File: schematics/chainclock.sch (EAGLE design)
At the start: 17 parts, among them SW1 ROTARTY_ENCODER

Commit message: Update layout
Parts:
- removed R11, R12, R5, R6: 10k, SparkFun-Resistors:RESISTOR2010
- added R1, R2, R7, R8: 10k, SparkFun-Resistors:RESISTOREZ
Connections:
- net 3V32: now also R1.2, R2.2; no longer R11.2, R12.2
- net N$2: now also R1.1, R7.2; no longer R11.1, R5.1
- net N$5: now also R2.1, R8.2; no longer R12.1, R6.2
- net RENCA: now also ARDUNOFIO.A1, R8.1; no longer ARDUNOFIO.D12, R6.1
- net RENCB: now also ARDUNOFIO.A2, R7.1; no longer ARDUNOFIO.D11, R5.2
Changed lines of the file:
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@@
 <part name="GND10" library="SparkFun-Aesthetics" deviceset="GND" device=""/>
 <part name="GND11" library="SparkFun-Aesthetics" deviceset="GND" device=""/>
-<part name="R11" library="SparkFun-Resistors" deviceset="RESISTOR" device="2010" value="10k"/>
-<part name="R12" library="SparkFun-Resistors" deviceset="RESISTOR" device="2010" value="10k"/>
 <part name="GND12" library="SparkFun-Aesthetics" deviceset="GND" device=""/>
-<part name="R5" library="SparkFun-Resistors" deviceset="RESISTOR" device="2010" value="10k"/>
-<part name="R6" library="SparkFun-Resistors" deviceset="RESISTOR" device="2010" value="10k"/>
 <part name="GND1" library="SparkFun-Aesthetics" deviceset="GND" device=""/>
 <part name="U$4" library="desjardins" deviceset="SG30XX" device="JC"/>
+<part name="R1" library="SparkFun-Resistors" deviceset="RESISTOR" device="EZ" value="10k"/>
+<part name="R2" library="SparkFun-Resistors" deviceset="RESISTOR" device="EZ" value="10k"/>
+<part name="R7" library="SparkFun-Resistors" deviceset="RESISTOR" device="EZ" value="10k"/>
+<part name="R8" library="SparkFun-Resistors" deviceset="RESISTOR" device="EZ" value="10k"/>
 </parts>
 <sheets>
@@
 <instance part="GND10" gate="1" x="91.44" y="81.28" rot="MR0"/>
 <instance part="GND11" gate="1" x="50.8" y="81.28" rot="MR0"/>
-<instance part="R11" gate="G$1" x="76.2" y="106.68" rot="MR90"/>
-<instance part="R12" gate="G$1" x="66.04" y="106.68" rot="MR90"/>
 <instance part="GND12" gate="1" x="66.04" y="68.58"/>
-<instance part="R5" gate="G$1" x="83.82" y="96.52" rot="MR180"/>
-<instance part="R6" gate="G$1" x="58.42" y="96.52" rot="MR180"/>
 <instance part="GND1" gate="1" x="88.9" y="149.86" rot="R270"/>
 <instance part="U$4" gate="G$1" x="106.68" y="154.94"/>
+<instance part="R1" gate="G$1" x="76.2" y="106.68" rot="R90"/>
+<instance part="R2" gate="G$1" x="66.04" y="106.68" rot="R90"/>
+<instance part="R7" gate="G$1" x="83.82" y="96.52" rot="R180"/>
+<instance part="R8" gate="G$1" x="58.42" y="96.52"/>
 </instances>
 <busses>
@@
 <junction x="71.12" y="114.3"/>
 <label x="48.26" y="127" size="1.778" layer="95"/>
-<pinref part="R11" gate="G$1" pin="2"/>
-<pinref part="R12" gate="G$1" pin="2"/>
+<pinref part="R2" gate="G$1" pin="2"/>
+<pinref part="R1" gate="G$1" pin="2"/>
+<label x="68.58" y="116.84" size="1.778" layer="95"/>
 </segment>
 <segment>
@@
 <pinref part="SW1" gate="G$1" pin="B"/>
 <wire x1="76.2" y1="93.98" x2="76.2" y2="96.52" width="0.1524" layer="91"/>
+<pinref part="R1" gate="G$1" pin="1"/>
+<pinref part="R7" gate="G$1" pin="2"/>
+<wire x1="76.2" y1="96.52" x2="76.2" y2="101.6" width="0.1524" layer="91"/>
 <wire x1="76.2" y1="96.52" x2="78.74" y2="96.52" width="0.1524" layer="91"/>
-<wire x1="76.2" y1="96.52" x2="76.2" y2="101.6" width="0.1524" layer="91"/>
 <junction x="76.2" y="96.52"/>
-<pinref part="R11" gate="G$1" pin="1"/>
-<pinref part="R5" gate="G$1" pin="1"/>
 </segment>
 </net>
@@
 <wire x1="66.04" y1="96.52" x2="66.04" y2="101.6" width="0.1524" layer="91"/>
 <junction x="66.04" y="96.52"/>
-<pinref part="R12" gate="G$1" pin="1"/>
-<pinref part="R6" gate="G$1" pin="2"/>
+<pinref part="R8" gate="G$1" pin="2"/>
+<pinref part="R2" gate="G$1" pin="1"/>
 </segment>
 </net>
 <net name="RENBTN" class="0">
+<segment>
+<pinref part="SW1" gate="G$1" pin="SW+"/>
+<wire x1="76.2" y1="73.66" x2="76.2" y2="71.12" width="0.1524" layer="91"/>
+<label x="73.66" y="68.58" size="1.778" layer="95"/>
+</segment>
 <segment>
 <pinref part="ARDUNOFIO" gate="G$1" pin="D6"/>
@@
 <label x="43.18" y="182.88" size="1.778" layer="95"/>
 </segment>
-<segment>
-<pinref part="SW1" gate="G$1" pin="SW+"/>
-<wire x1="76.2" y1="73.66" x2="76.2" y2="71.12" width="0.1524" layer="91"/>
-<label x="73.66" y="68.58" size="1.778" layer="95"/>
-</segment>
 </net>
 <net name="RENCB" class="0">
 <segment>
-<pinref part="ARDUNOFIO" gate="G$1" pin="D11"/>
-<wire x1="43.18" y1="195.58" x2="45.72" y2="195.58" width="0.1524" layer="91"/>
-<label x="43.18" y="195.58" size="1.778" layer="95"/>
-</segment>
-<segment>
-<wire x1="88.9" y1="96.52" x2="91.44" y2="96.52" width="0.1524" layer="91"/>
 <wire x1="91.44" y1="96.52" x2="93.98" y2="96.52" width="0.1524" layer="91"/>
 <wire x1="91.44" y1="96.52" x2="91.44" y2="93.98" width="0.1524" layer="91"/>
-<junction x="91.44" y="96.52"/>
 <pinref part="C6" gate="G$1" pin="1"/>
 <label x="101.6" y="96.52" size="1.778" layer="95" rot="MR0"/>
-<pinref part="R5" gate="G$1" pin="2"/>
+<pinref part="R7" gate="G$1" pin="1"/>
+<wire x1="91.44" y1="96.52" x2="88.9" y2="96.52" width="0.1524" layer="91"/>
+<junction x="91.44" y="96.52"/>
+</segment>
+<segment>
+<pinref part="ARDUNOFIO" gate="G$1" pin="A2"/>
+<wire x1="12.7" y1="187.96" x2="10.16" y2="187.96" width="0.1524" layer="91"/>
+<label x="5.08" y="187.96" size="1.778" layer="95"/>
 </segment>
 </net>
 <net name="RENCA" class="0">
-<segment>
-<pinref part="ARDUNOFIO" gate="G$1" pin="D12"/>
-<wire x1="43.18" y1="198.12" x2="45.72" y2="198.12" width="0.1524" layer="91"/>
-<label x="43.18" y="198.12" size="1.778" layer="95"/>
-</segment>
 <segment>
 <wire x1="53.34" y1="96.52" x2="50.8" y2="96.52" width="0.1524" layer="91"/>
@@
 <pinref part="C5" gate="G$1" pin="1"/>
 <label x="48.26" y="96.52" size="1.778" layer="95" rot="MR0"/>
-<pinref part="R6" gate="G$1" pin="1"/>
-</segment>
-</net>
+<pinref part="R8" gate="G$1" pin="1"/>
+</segment>
+<segment>
+<pinref part="ARDUNOFIO" gate="G$1" pin="A1"/>
+<wire x1="12.7" y1="185.42" x2="10.16" y2="185.42" width="0.1524" layer="91"/>
+<label x="5.08" y="185.42" size="1.778" layer="95"/>
+</segment>
+</net>

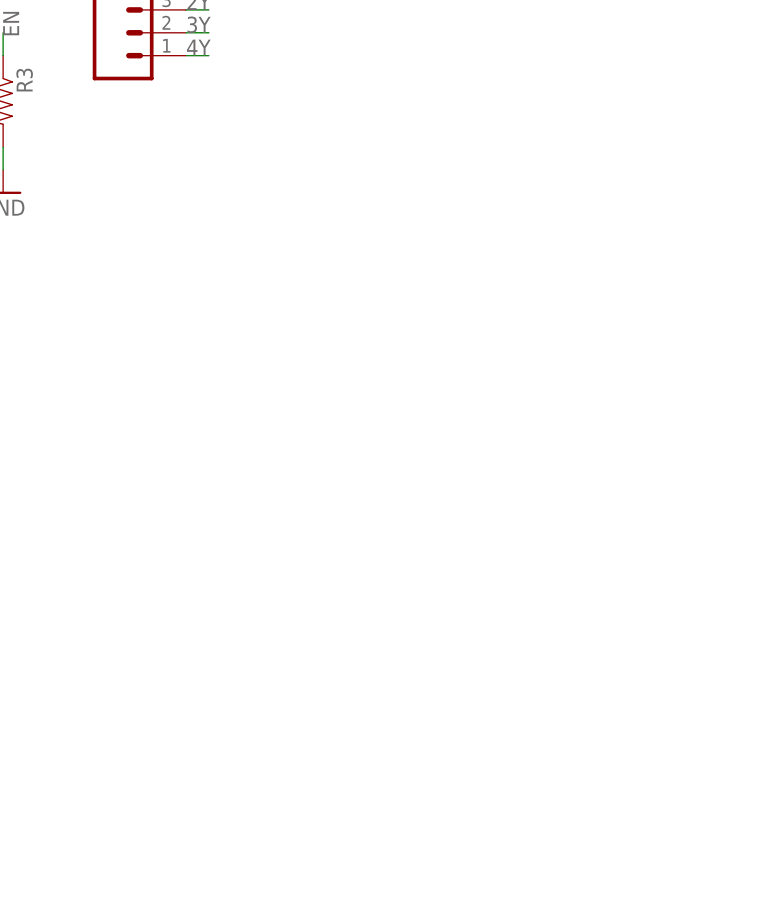
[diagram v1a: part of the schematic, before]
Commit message: Add voltage limiter for solar
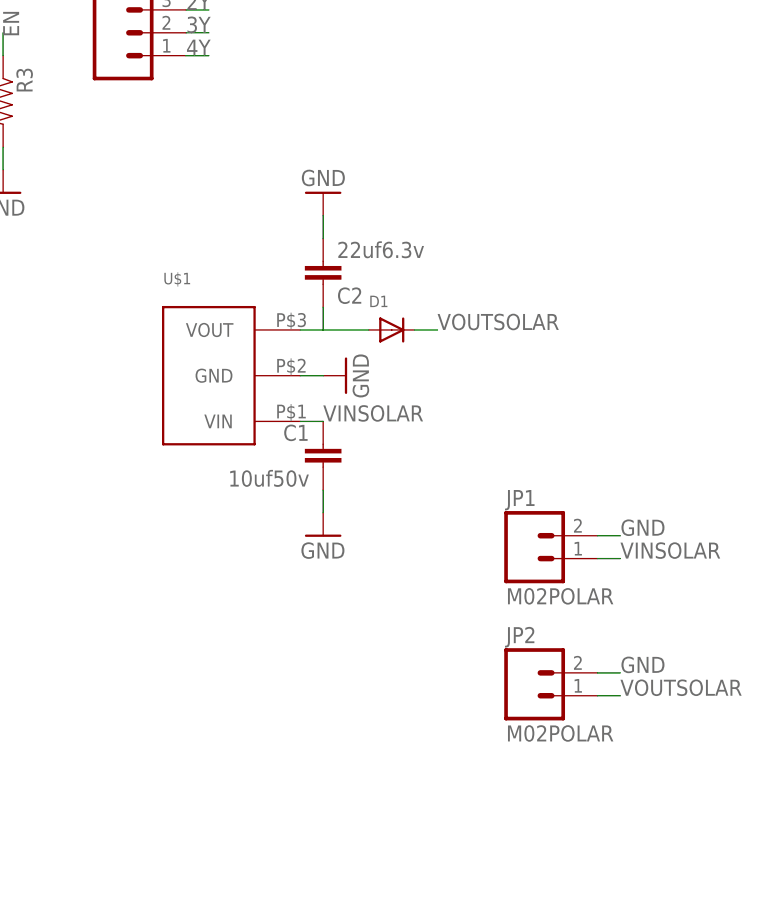
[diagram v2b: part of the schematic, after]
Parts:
- added C1: 10uf50v, SparkFun-Capacitors:CAPKIT
- added C2: 22uf6.3v, SparkFun-Capacitors:CAPKIT
- added D1: (no value), adafruit:DIODEDO-1N4148
- added JP1, JP2: M02POLAR, desjardins:M02POLAR
- added U$1: V78-500, desjardins:V78-500
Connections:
- new net N$4: C2.1, D1.A, U$1.VOUT
- new net VINSOLAR: C1.1, JP1.1, U$1.VIN
- new net VOUTSOLAR: D1.C, JP2.1
- net GND: now also C1.2, C2.2, JP1.2, JP2.2, U$1.GND
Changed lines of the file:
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@@
 <part name="R7" library="SparkFun-Resistors" deviceset="RESISTOR" device="EZ" value="10k"/>
 <part name="R8" library="SparkFun-Resistors" deviceset="RESISTOR" device="EZ" value="10k"/>
+<part name="U$1" library="desjardins" deviceset="V78-500" device=""/>
+<part name="C1" library="SparkFun-Capacitors" deviceset="CAP" device="KIT" value="10uf50v"/>
+<part name="C2" library="SparkFun-Capacitors" deviceset="CAP" device="KIT" value="22uf6.3v"/>
+<part name="GND9" library="SparkFun-Aesthetics" deviceset="GND" device=""/>
+<part name="GND13" library="SparkFun-Aesthetics" deviceset="GND" device=""/>
+<part name="GND14" library="SparkFun-Aesthetics" deviceset="GND" device=""/>
+<part name="D1" library="adafruit" deviceset="DIODE" device="DO-1N4148"/>
+<part name="JP1" library="desjardins" deviceset="M02" device="POLAR"/>
+<part name="JP2" library="desjardins" deviceset="M02" device="POLAR"/>
 </parts>
 <sheets>
@@
 <instance part="R7" gate="G$1" x="83.82" y="96.52" rot="R180"/>
 <instance part="R8" gate="G$1" x="58.42" y="96.52"/>
+<instance part="U$1" gate="G$1" x="213.36" y="154.94"/>
+<instance part="C1" gate="G$1" x="226.06" y="144.78" rot="MR0"/>
+<instance part="C2" gate="G$1" x="226.06" y="167.64" rot="MR180"/>
+<instance part="GND9" gate="1" x="226.06" y="137.16"/>
+<instance part="GND13" gate="1" x="226.06" y="175.26" rot="R180"/>
+<instance part="GND14" gate="1" x="228.6" y="154.94" rot="R90"/>
+<instance part="D1" gate="G$1" x="233.68" y="160.02"/>
+<instance part="JP1" gate="G$1" x="248.92" y="134.62"/>
+<instance part="JP2" gate="G$1" x="248.92" y="119.38"/>
 </instances>
 <busses>
@@
 <pinref part="GND1" gate="1" pin="GND"/>
 <pinref part="U$4" gate="G$1" pin="GND"/>
+</segment>
+<segment>
+<pinref part="U$1" gate="G$1" pin="GND"/>
+<wire x1="223.52" y1="154.94" x2="226.06" y2="154.94" width="0.1524" layer="91"/>
+<pinref part="GND14" gate="1" pin="GND"/>
+</segment>
+<segment>
+<wire x1="256.54" y1="137.16" x2="259.08" y2="137.16" width="0.1524" layer="91"/>
+<label x="259.08" y="137.16" size="1.778" layer="95"/>
+<pinref part="JP1" gate="G$1" pin="2"/>
+</segment>
+<segment>
+<wire x1="256.54" y1="121.92" x2="259.08" y2="121.92" width="0.1524" layer="91"/>
+<label x="259.08" y="121.92" size="1.778" layer="95"/>
+<pinref part="JP2" gate="G$1" pin="2"/>
+</segment>
+<segment>
+<pinref part="C1" gate="G$1" pin="2"/>
+<wire x1="226.06" y1="142.24" x2="226.06" y2="139.7" width="0.1524" layer="91"/>
+<pinref part="GND9" gate="1" pin="GND"/>
+</segment>
+<segment>
+<pinref part="C2" gate="G$1" pin="2"/>
+<wire x1="226.06" y1="170.18" x2="226.06" y2="172.72" width="0.1524" layer="91"/>
+<pinref part="GND13" gate="1" pin="GND"/>
 </segment>
 </net>
@@
 </segment>
 </net>
+<net name="VOUTSOLAR" class="0">
+<segment>
+<wire x1="256.54" y1="119.38" x2="259.08" y2="119.38" width="0.1524" layer="91"/>
+<label x="259.08" y="119.38" size="1.778" layer="95"/>
+<pinref part="JP2" gate="G$1" pin="1"/>
+</segment>
+<segment>
+<pinref part="D1" gate="G$1" pin="C"/>
+<wire x1="236.22" y1="160.02" x2="238.76" y2="160.02" width="0.1524" layer="91"/>
+<label x="238.76" y="160.02" size="1.778" layer="95"/>
+</segment>
+</net>
+<net name="VINSOLAR" class="0">
+<segment>
+<pinref part="U$1" gate="G$1" pin="VIN"/>
+<wire x1="223.52" y1="149.86" x2="226.06" y2="149.86" width="0.1524" layer="91"/>
+<label x="226.06" y="149.86" size="1.778" layer="95"/>
+<pinref part="C1" gate="G$1" pin="1"/>
+</segment>
+<segment>
+<wire x1="256.54" y1="134.62" x2="259.08" y2="134.62" width="0.1524" layer="91"/>
+<label x="259.08" y="134.62" size="1.778" layer="95"/>
+<pinref part="JP1" gate="G$1" pin="1"/>
+</segment>
+</net>
+<net name="N$4" class="0">
+<segment>
+<pinref part="U$1" gate="G$1" pin="VOUT"/>
+<pinref part="D1" gate="G$1" pin="A"/>
+<wire x1="223.52" y1="160.02" x2="226.06" y2="160.02" width="0.1524" layer="91"/>
+<pinref part="C2" gate="G$1" pin="1"/>
+<wire x1="226.06" y1="160.02" x2="231.14" y2="160.02" width="0.1524" layer="91"/>
+<wire x1="226.06" y1="160.02" x2="226.06" y2="162.56" width="0.1524" layer="91"/>
+</segment>
+</net>

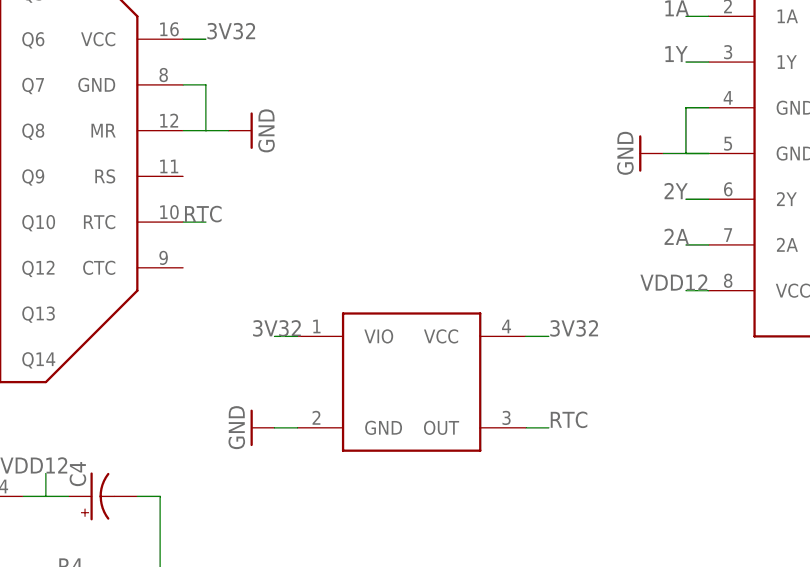
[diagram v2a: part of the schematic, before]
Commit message: Updates to the counter
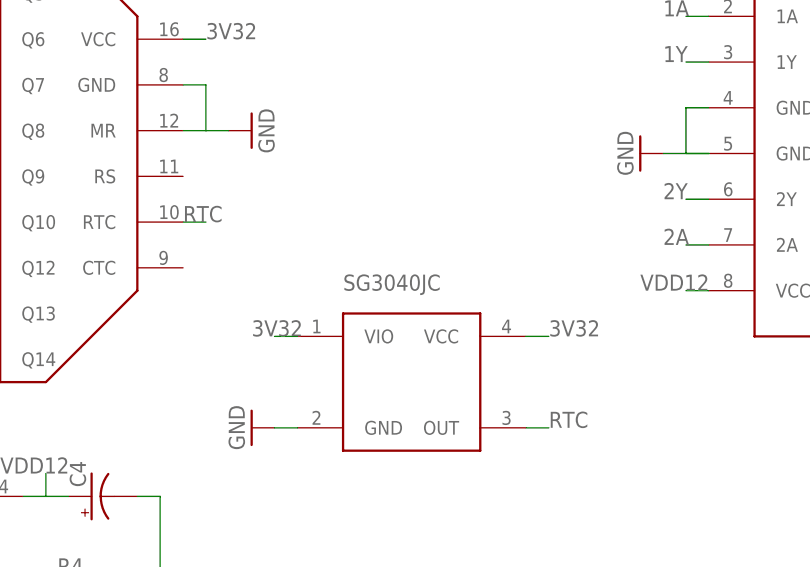
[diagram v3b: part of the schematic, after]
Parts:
- renumbered U$4 to SG3040JC
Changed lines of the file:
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@@
 <part name="GND12" library="SparkFun-Aesthetics" deviceset="GND" device=""/>
 <part name="GND1" library="SparkFun-Aesthetics" deviceset="GND" device=""/>
-<part name="U$4" library="desjardins" deviceset="SG30XX" device="JC"/>
+<part name="SG3040JC" library="desjardins" deviceset="SG30XX" device="JC"/>
 <part name="R1" library="SparkFun-Resistors" deviceset="RESISTOR" device="EZ" value="10k"/>
 <part name="R2" library="SparkFun-Resistors" deviceset="RESISTOR" device="EZ" value="10k"/>
@@
 <instance part="GND12" gate="1" x="66.04" y="68.58"/>
 <instance part="GND1" gate="1" x="88.9" y="149.86" rot="R270"/>
-<instance part="U$4" gate="G$1" x="106.68" y="154.94"/>
+<instance part="SG3040JC" gate="G$1" x="106.68" y="154.94"/>
 <instance part="R1" gate="G$1" x="76.2" y="106.68" rot="R90"/>
 <instance part="R2" gate="G$1" x="66.04" y="106.68" rot="R90"/>
@@
 <wire x1="93.98" y1="149.86" x2="91.44" y2="149.86" width="0.1524" layer="91"/>
 <pinref part="GND1" gate="1" pin="GND"/>
-<pinref part="U$4" gate="G$1" pin="GND"/>
+<pinref part="SG3040JC" gate="G$1" pin="GND"/>
 </segment>
 <segment>
@@
 <wire x1="119.38" y1="160.02" x2="121.92" y2="160.02" width="0.1524" layer="91"/>
 <label x="121.92" y="160.02" size="1.778" layer="95"/>
-<pinref part="U$4" gate="G$1" pin="VCC"/>
+<pinref part="SG3040JC" gate="G$1" pin="VCC"/>
 </segment>
 <segment>
 <wire x1="93.98" y1="160.02" x2="91.44" y2="160.02" width="0.1524" layer="91"/>
 <label x="88.9" y="160.02" size="1.778" layer="95"/>
-<pinref part="U$4" gate="G$1" pin="VIO"/>
+<pinref part="SG3040JC" gate="G$1" pin="VIO"/>
 </segment>
 </net>
@@
 <wire x1="119.38" y1="149.86" x2="121.92" y2="149.86" width="0.1524" layer="91"/>
 <label x="121.92" y="149.86" size="1.778" layer="95"/>
-<pinref part="U$4" gate="G$1" pin="OUT"/>
-</segment>
-</net>
+<pinref part="SG3040JC" gate="G$1" pin="OUT"/>
+</segment>
+</net>
